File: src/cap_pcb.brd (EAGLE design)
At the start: 36 x 70 mm, 20 parts, among them CON1 PINHEAD_2X02-PTH-2-MALE, CON2 PINHEAD_2X02-PTH-2-MALE, CON3 PINHEAD_2X02-PTH-2-MALE, CON4 PINHEAD_2X02-PTH-2-MALE

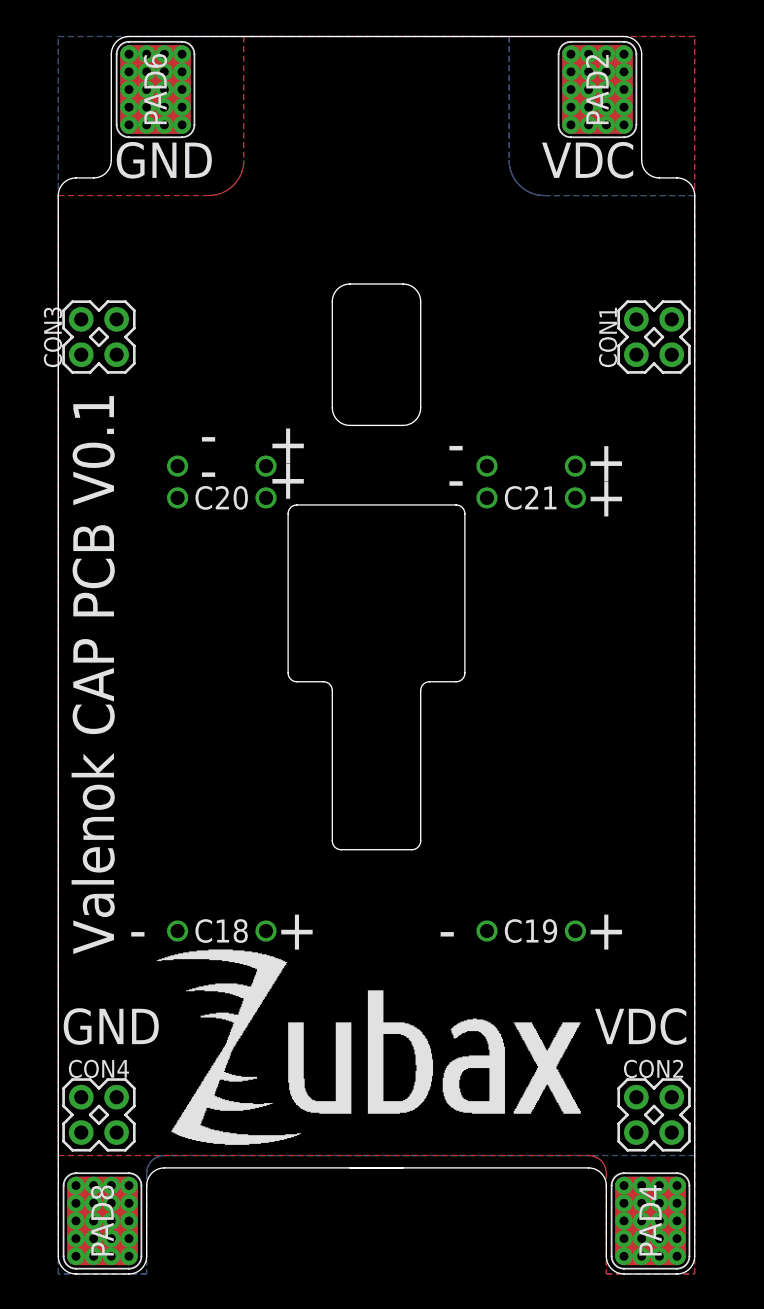
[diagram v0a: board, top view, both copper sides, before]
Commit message: Massive routing update
InterPCB connectors between Cap PCB and power PCB replaced with bigger ones
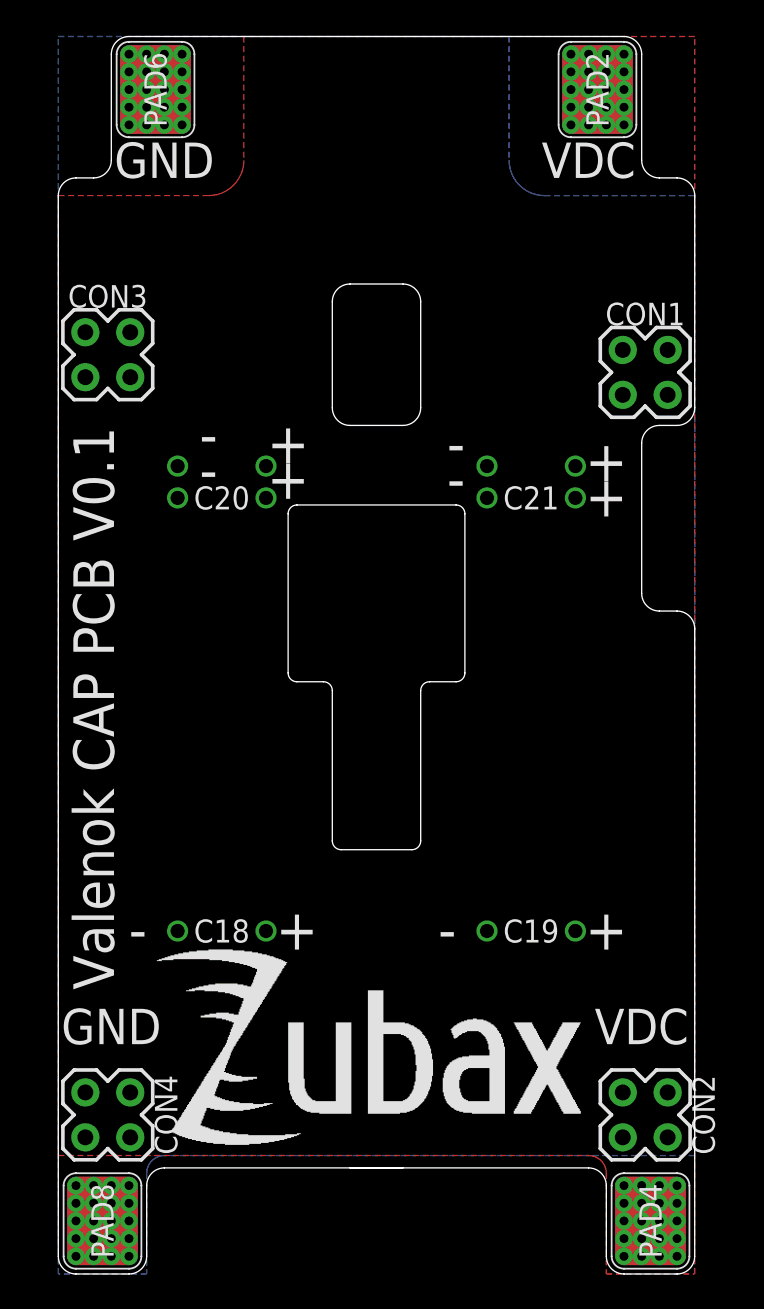
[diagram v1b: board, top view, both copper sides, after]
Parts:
- CON1, CON2, CON3, CON4: value PINHEAD_2X02-PTH-2-MALE -> PINHEAD_2X02-PTH-2.54-MALE; device pinhead:2X02-PTH-2 -> pinhead:2X02-PTH-2.54
- moved CON1 2.06 mm to (15.2, 55.0)
- moved CON3 1.12 mm to (-15.2, 56.0)
- moved CON2 0.50 mm to (15.2, 13.0)
- moved CON4 0.50 mm to (-15.2, 13.0)
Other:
- outline, holes or cut-outs redrawn
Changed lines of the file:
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@@
 <setting verticaltext="up"/>
 </settings>
-<grid distance="3" unitdist="mm" unit="mm" style="lines" multiple="1" display="yes" altdistance="5" altunitdist="mil" altunit="mil"/>
+<grid distance="0.5" unitdist="mm" unit="mm" style="lines" multiple="1" display="yes" altdistance="5" altunitdist="mil" altunit="mil"/>
 <layers>
 <layer number="1" name="Top" color="4" fill="1" visible="yes" active="yes"/>
@@
 <wire x1="0" y1="0" x2="0" y2="80" width="0.01" layer="47" style="shortdash" locked="yes"/>
 <wire x1="-18" y1="65" x2="-18" y2="5" width="0.01" layer="20"/>
-<wire x1="18" y1="65" x2="18" y2="5" width="0.01" layer="20"/>
+<wire x1="18" y1="65" x2="18" y2="53" width="0.01" layer="20"/>
+<wire x1="18" y1="53" x2="17" y2="52" width="0.01" layer="20" curve="-90"/>
+<wire x1="17" y1="52" x2="16" y2="52" width="0.01" layer="20"/>
+<wire x1="16" y1="41.5" x2="17" y2="41.5" width="0.01" layer="20"/>
+<wire x1="17" y1="41.5" x2="18" y2="40.5" width="0.01" layer="20" curve="-90"/>
+<wire x1="18" y1="40.5" x2="18" y2="5" width="0.01" layer="20"/>
 <wire x1="-13" y1="5" x2="-13" y2="9" width="0.01" layer="20"/>
 <wire x1="-13" y1="9" x2="-12" y2="10" width="0.01" layer="20" curve="-90"/>
@@
 <text x="15" y="18" size="2" layer="22" font="vector" ratio="15" rot="MR0" align="center">VDC</text>
 <text x="-15" y="18" size="2" layer="22" font="vector" ratio="15" rot="MR0" align="center">GND</text>
-<text x="-16" y="38" size="2.3" layer="21" font="vector" ratio="15" rot="R90" align="center">Valenok CAP PCB V0.1</text>
+<text x="-16" y="36" size="2.3" layer="21" font="vector" ratio="15" rot="R90" align="center">Valenok CAP PCB V0.1</text>
 <text x="-5" y="51" size="2.3" layer="21" font="vector" ratio="15" align="center">+</text>
 <text x="-5" y="49" size="2.3" layer="21" font="vector" ratio="15" align="center">+</text>
@@
 <text x="4" y="23.5" size="2.3" layer="21" font="vector" ratio="15" align="center">-</text>
 <text x="-13.5" y="23.5" size="2.3" layer="21" font="vector" ratio="15" align="center">-</text>
+<wire x1="16" y1="52" x2="15" y2="51" width="0.01" layer="20" curve="90"/>
+<wire x1="15" y1="51" x2="15" y2="42.5" width="0.01" layer="20"/>
+<wire x1="15" y1="42.5" x2="16" y2="41.5" width="0.01" layer="20" curve="90"/>
 </plain>
 <attributes>
@@
 <attribute name="VOLTAGE" value="160V" x="8.75" y="47.9" size="1.778" layer="27" rot="R180" display="off"/>
 </element>
-<element name="CON3" library="pinhead" library_urn="urn:adsk.eagle:library:2540341" package="2X02-PTH-2" package3d_urn="urn:adsk.eagle:package:23506355/2" value="PINHEAD_2X02-PTH-2-MALE" x="-15.7" y="57" smashed="yes" rot="R90">
-<attribute name="NAME" x="-18.3" y="57" size="1" layer="25" font="vector" ratio="15" rot="R90" align="center"/>
-</element>
-<element name="CON1" library="pinhead" library_urn="urn:adsk.eagle:library:2540341" package="2X02-PTH-2" package3d_urn="urn:adsk.eagle:package:23506355/2" value="PINHEAD_2X02-PTH-2-MALE" x="15.7" y="57" smashed="yes" rot="R90">
-<attribute name="NAME" x="13.1" y="57" size="1" layer="25" font="vector" ratio="15" rot="R90" align="center"/>
-</element>
-<element name="CON2" library="pinhead" library_urn="urn:adsk.eagle:library:2540341" package="2X02-PTH-2" package3d_urn="urn:adsk.eagle:package:23506355/2" value="PINHEAD_2X02-PTH-2-MALE" x="15.7" y="13" smashed="yes">
-<attribute name="NAME" x="15.7" y="15.6" size="1" layer="25" font="vector" ratio="15" align="center"/>
-</element>
-<element name="CON4" library="pinhead" library_urn="urn:adsk.eagle:library:2540341" package="2X02-PTH-2" package3d_urn="urn:adsk.eagle:package:23506355/2" value="PINHEAD_2X02-PTH-2-MALE" x="-15.7" y="13" smashed="yes">
-<attribute name="NAME" x="-15.7" y="15.6" size="1" layer="25" font="vector" ratio="15" align="center"/>
+<element name="CON3" library="pinhead" library_urn="urn:adsk.eagle:library:2540341" package="2X02-PTH-2.54" package3d_urn="urn:adsk.eagle:package:24957333/1" value="PINHEAD_2X02-PTH-2.54-MALE" x="-15.2" y="56" smashed="yes" rot="R90">
+<attribute name="NAME" x="-15.2" y="59.302" size="1.27" layer="25" font="vector" ratio="15" align="center"/>
+</element>
+<element name="CON1" library="pinhead" library_urn="urn:adsk.eagle:library:2540341" package="2X02-PTH-2.54" package3d_urn="urn:adsk.eagle:package:24957333/1" value="PINHEAD_2X02-PTH-2.54-MALE" x="15.2" y="55" smashed="yes" rot="R90">
+<attribute name="NAME" x="15.2" y="58.302" size="1.27" layer="25" font="vector" ratio="15" align="center"/>
+</element>
+<element name="CON2" library="pinhead" library_urn="urn:adsk.eagle:library:2540341" package="2X02-PTH-2.54" package3d_urn="urn:adsk.eagle:package:24957333/1" value="PINHEAD_2X02-PTH-2.54-MALE" x="15.2" y="13" smashed="yes">
+<attribute name="NAME" x="18.502" y="13" size="1.27" layer="25" font="vector" ratio="15" rot="R270" align="center"/>
+</element>
+<element name="CON4" library="pinhead" library_urn="urn:adsk.eagle:library:2540341" package="2X02-PTH-2.54" package3d_urn="urn:adsk.eagle:package:24957333/1" value="PINHEAD_2X02-PTH-2.54-MALE" x="-15.2" y="13" smashed="yes">
+<attribute name="NAME" x="-11.898" y="13" size="1.27" layer="25" font="vector" ratio="15" rot="R270" align="center"/>
 </element>
 <element name="PAD4" library="PADS" library_urn="urn:adsk.eagle:library:3188696" package="5X4" package3d_urn="urn:adsk.eagle:package:5210040/1" value="PAD-5X4" x="15.5" y="7" smashed="yes" rot="R90">

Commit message: assembly variant fix
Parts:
- removed U$1: (no value), logo:ZUBAX_25X12
- added U$3: (no value), logo:ZUBAX_20X9
- flipped CON1 to the bottom
- flipped CON2 to the bottom
- flipped CON3 to the bottom
- flipped CON4 to the bottom
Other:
- outline, holes or cut-outs redrawn

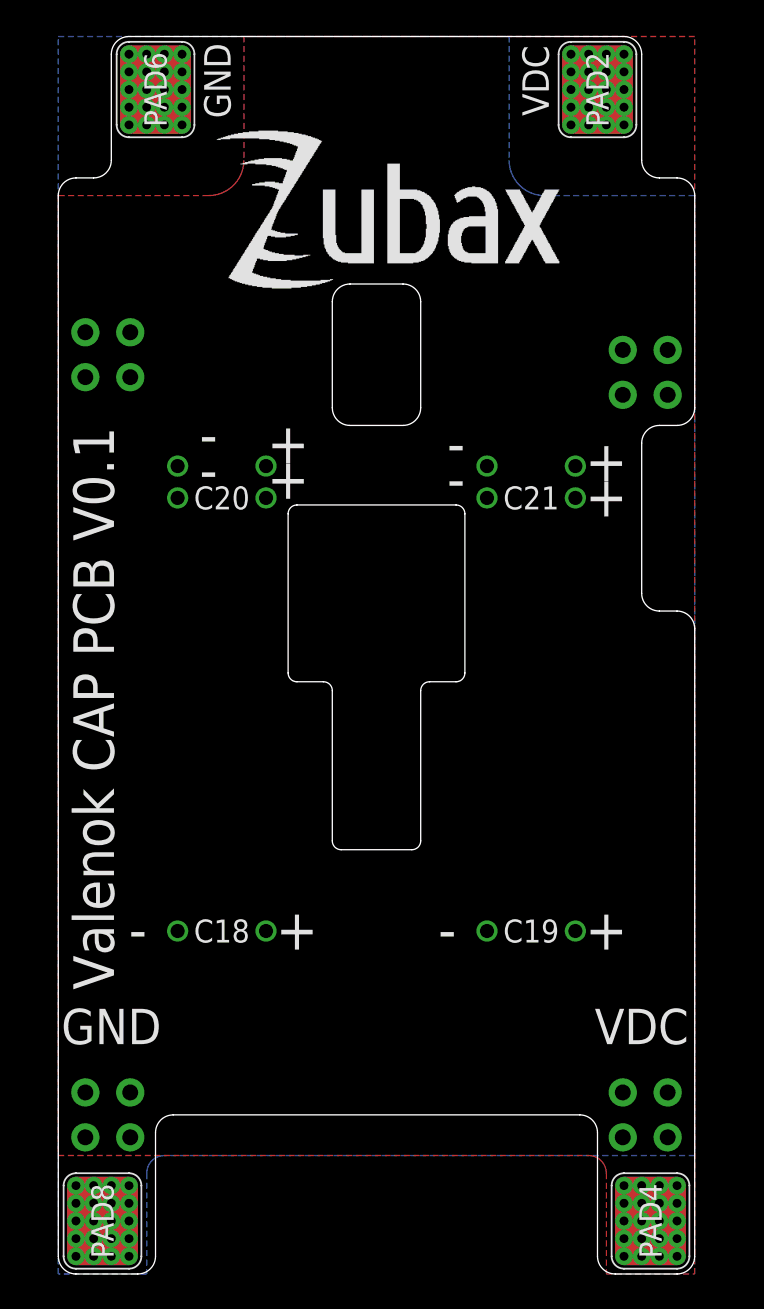
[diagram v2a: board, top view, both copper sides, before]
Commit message: Outline updates to allow debug assembly with connectors
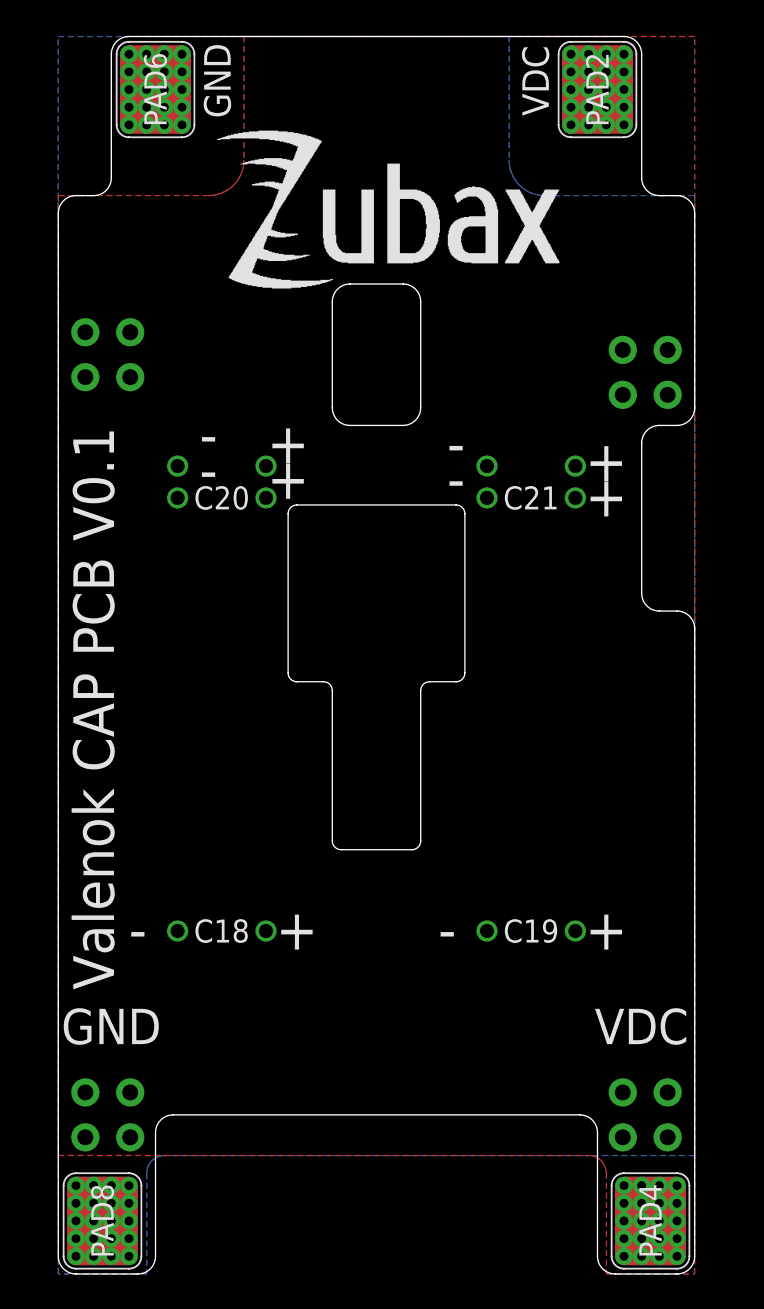
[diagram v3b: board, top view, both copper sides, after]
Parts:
- removed U$2: (no value), logo:ZUBAX_25X12
- added U$1: (no value), logo:ZUBAX_20X9
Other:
- outline, holes or cut-outs redrawn
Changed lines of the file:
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@@
 <setting verticaltext="up"/>
 </settings>
-<grid distance="0.5" unitdist="mm" unit="mm" style="lines" multiple="1" display="yes" altdistance="5" altunitdist="mil" altunit="mil"/>
+<grid distance="1" unitdist="mm" unit="mm" style="lines" multiple="1" display="yes" altdistance="5" altunitdist="mil" altunit="mil"/>
 <layers>
-<layer number="1" name="Top" color="4" fill="1" visible="no" active="yes"/>
+<layer number="1" name="Top" color="4" fill="1" visible="yes" active="yes"/>
 <layer number="2" name="Route2" color="16" fill="1" visible="no" active="yes"/>
 <layer number="3" name="Route3" color="17" fill="1" visible="no" active="no"/>
@@
 <layer number="14" name="Route14" color="22" fill="1" visible="no" active="no"/>
 <layer number="15" name="Route15" color="23" fill="1" visible="no" active="yes"/>
-<layer number="16" name="Bottom" color="1" fill="1" visible="yes" active="yes"/>
+<layer number="16" name="Bottom" color="1" fill="1" visible="no" active="yes"/>
 <layer number="17" name="Pads" color="2" fill="1" visible="yes" active="yes"/>
 <layer number="18" name="Vias" color="2" fill="1" visible="yes" active="yes"/>
 <layer number="19" name="Unrouted" color="6" fill="1" visible="no" active="yes"/>
 <layer number="20" name="Dimension" color="24" fill="1" visible="yes" active="yes"/>
-<layer number="21" name="tPlace" color="7" fill="1" visible="no" active="yes"/>
-<layer number="22" name="bPlace" color="7" fill="1" visible="yes" active="yes"/>
-<layer number="23" name="tOrigins" color="15" fill="1" visible="no" active="yes"/>
-<layer number="24" name="bOrigins" color="15" fill="1" visible="yes" active="yes"/>
-<layer number="25" name="tNames" color="7" fill="1" visible="no" active="yes"/>
-<layer number="26" name="bNames" color="7" fill="1" visible="yes" active="yes"/>
+<layer number="21" name="tPlace" color="7" fill="1" visible="yes" active="yes"/>
+<layer number="22" name="bPlace" color="7" fill="1" visible="no" active="yes"/>
+<layer number="23" name="tOrigins" color="15" fill="1" visible="yes" active="yes"/>
+<layer number="24" name="bOrigins" color="15" fill="1" visible="no" active="yes"/>
+<layer number="25" name="tNames" color="7" fill="1" visible="yes" active="yes"/>
+<layer number="26" name="bNames" color="7" fill="1" visible="no" active="yes"/>
 <layer number="27" name="tValues" color="7" fill="1" visible="no" active="yes"/>
 <layer number="28" name="bValues" color="7" fill="1" visible="no" active="yes"/>
@@
 <layer number="49" name="Reference" color="7" fill="1" visible="no" active="yes"/>
 <layer number="50" name="dxf" color="7" fill="1" visible="no" active="no"/>
-<layer number="51" name="tDocu" color="7" fill="1" visible="no" active="yes"/>
-<layer number="52" name="bDocu" color="7" fill="1" visible="yes" active="yes"/>
+<layer number="51" name="tDocu" color="7" fill="1" visible="yes" active="yes"/>
+<layer number="52" name="bDocu" color="7" fill="1" visible="no" active="yes"/>
 <layer number="53" name="tGND_GNDA" color="7" fill="9" visible="no" active="no"/>
 <layer number="54" name="bGND_GNDA" color="1" fill="9" visible="no" active="no"/>
@@
 </layers>
 <board>
-<fusionsync huburn="a.cGVyc29uYWw6dWUyYWE4ZDY4" projecturn="a.cGVyc29uYWw6dWUyYWE4ZDY4IzIwMjAwOTI1MzM2NDYxMjgx" f3durn="urn:adsk.wipprod:dm.lineage:IhySjAM5SyGK940RRZt57A" pcbguid="" lastpulledtime="" lastsyncedchangeguid="" latestrevisionid="19d2ab2a-8ab5-4abd-8e8b-b2554e491ade" lastsyncedrevisionid="19d2ab2a-8ab5-4abd-8e8b-b2554e491ade" lastboardhashguid="a488ca65-a204-448b-86b2-c1786aef74a6" lastpushedtime="2020-11-25T11:35:04Z" linktopcb3d="true"/>
+<fusionsync huburn="a.cGVyc29uYWw6dWUyYWE4ZDY4" projecturn="a.cGVyc29uYWw6dWUyYWE4ZDY4IzIwMjAwOTI1MzM2NDYxMjgx" f3durn="urn:adsk.wipprod:dm.lineage:IhySjAM5SyGK940RRZt57A" pcbguid="" lastpulledtime="" lastsyncedchangeguid="" latestrevisionid="b3880e43-36e1-41f6-b7b3-a77e92d007cd" lastsyncedrevisionid="b3880e43-36e1-41f6-b7b3-a77e92d007cd" lastboardhashguid="94f5aaa0-dff7-dc0e-3df6-afbb954c8df5" lastpushedtime="2020-11-25T12:14:18Z" linktopcb3d="true"/>
 <plain>
 <wire x1="0" y1="0" x2="0" y2="80" width="0.01" layer="47" style="shortdash" locked="yes"/>
-<wire x1="-18" y1="65" x2="-18" y2="5" width="0.01" layer="20"/>
-<wire x1="18" y1="65" x2="18" y2="53" width="0.01" layer="20"/>
+<wire x1="-15" y1="73" x2="-15" y2="66" width="0.01" layer="20"/>
+<wire x1="-15" y1="66" x2="-16" y2="65" width="0.01" layer="20" curve="-90"/>
+<wire x1="-16" y1="65" x2="-17" y2="65" width="0.01" layer="20"/>
+<wire x1="-17" y1="65" x2="-18" y2="64" width="0.01" layer="20" curve="90"/>
+<wire x1="-18" y1="64" x2="-18" y2="5" width="0.01" layer="20"/>
+<wire x1="15" y1="73" x2="15" y2="66" width="0.01" layer="20"/>
+<wire x1="15" y1="66" x2="16" y2="65" width="0.01" layer="20" curve="90"/>
+<wire x1="16" y1="65" x2="17" y2="65" width="0.01" layer="20"/>
+<wire x1="17" y1="65" x2="18" y2="64" width="0.01" layer="20" curve="-90"/>
+<wire x1="18" y1="64" x2="18" y2="53" width="0.01" layer="20"/>
 <wire x1="18" y1="53" x2="17" y2="52" width="0.01" layer="20" curve="-90"/>
 <wire x1="17" y1="52" x2="16" y2="52" width="0.01" layer="20"/>
@@
 <wire x1="12.5" y1="5" x2="13.5" y2="4" width="0.01" layer="20" curve="90"/>
 <wire x1="13.5" y1="4" x2="17" y2="4" width="0.01" layer="20"/>
-<wire x1="16" y1="66" x2="17" y2="66" width="0.01" layer="20"/>
-<wire x1="17" y1="66" x2="18" y2="65" width="0.01" layer="20" curve="-90"/>
 <wire x1="14" y1="74" x2="-14" y2="74" width="0.01" layer="20"/>
 <wire x1="-14" y1="74" x2="-15" y2="73" width="0.01" layer="20" curve="90"/>
-<wire x1="-15" y1="73" x2="-15" y2="67" width="0.01" layer="20"/>
-<wire x1="-15" y1="67" x2="-16" y2="66" width="0.01" layer="20" curve="-90"/>
-<wire x1="-16" y1="66" x2="-17" y2="66" width="0.01" layer="20"/>
 <wire x1="14" y1="74" x2="15" y2="73" width="0.01" layer="20" curve="-90"/>
-<wire x1="15" y1="73" x2="15" y2="67" width="0.01" layer="20"/>
-<wire x1="15" y1="67" x2="16" y2="66" width="0.01" layer="20" curve="90"/>
-<wire x1="-17" y1="66" x2="-18" y2="65" width="0.01" layer="20" curve="90"/>
 <rectangle x1="-2.5" y1="62" x2="2.5" y2="70" layer="49"/>
 <rectangle x1="-2.5" y1="36" x2="2.5" y2="44" layer="49"/>
@@
 <attribute name="NAME" x="-15.5" y="7" size="1.27" layer="25" font="vector" ratio="15" rot="R90" align="center"/>
 </element>
-<element name="U$2" library="logo" library_urn="urn:adsk.eagle:library:6668987" package="ZUBAX_25X12" package3d_urn="urn:adsk.eagle:package:11612839/1" value="" x="13" y="11" smashed="yes" rot="MR0"/>
 <element name="U$3" library="logo" library_urn="urn:adsk.eagle:library:6668987" package="ZUBAX_20X9" package3d_urn="urn:adsk.eagle:package:11612844/1" value="" x="-9.5" y="59.5" smashed="yes"/>
+<element name="U$1" library="logo" library_urn="urn:adsk.eagle:library:6668987" package="ZUBAX_20X9" package3d_urn="urn:adsk.eagle:package:11612844/1" value="" x="11.5" y="13.5" smashed="yes" rot="MR0"/>
 </elements>
 <signals>
